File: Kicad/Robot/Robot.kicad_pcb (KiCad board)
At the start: 2 copper layers, 36 parts, among them J1 X8R HEADER, J10 LightBar1, J11 LightBar2, J12 PIN HEADER DE0-NANO POWER, J2 LORA, J3 RELAY HEADER, J4 SENSOR 1, J5 SENSOR 2, J6 SENSOR 3, J7 SENSOR 4, J8 MotorDriver1, J9 MotorDriver2, U1 USB_POWER, U2 Generic_DC_to_DC_Module, U3 Generic_DC_to_DC_Module, U4 Generic_DC_to_DC_Module, U5 Generic_DC_to_DC_Module, U6 X8R_Receiver, U7 TXS0108E, U8 RFM9X, U9 TDB62381A

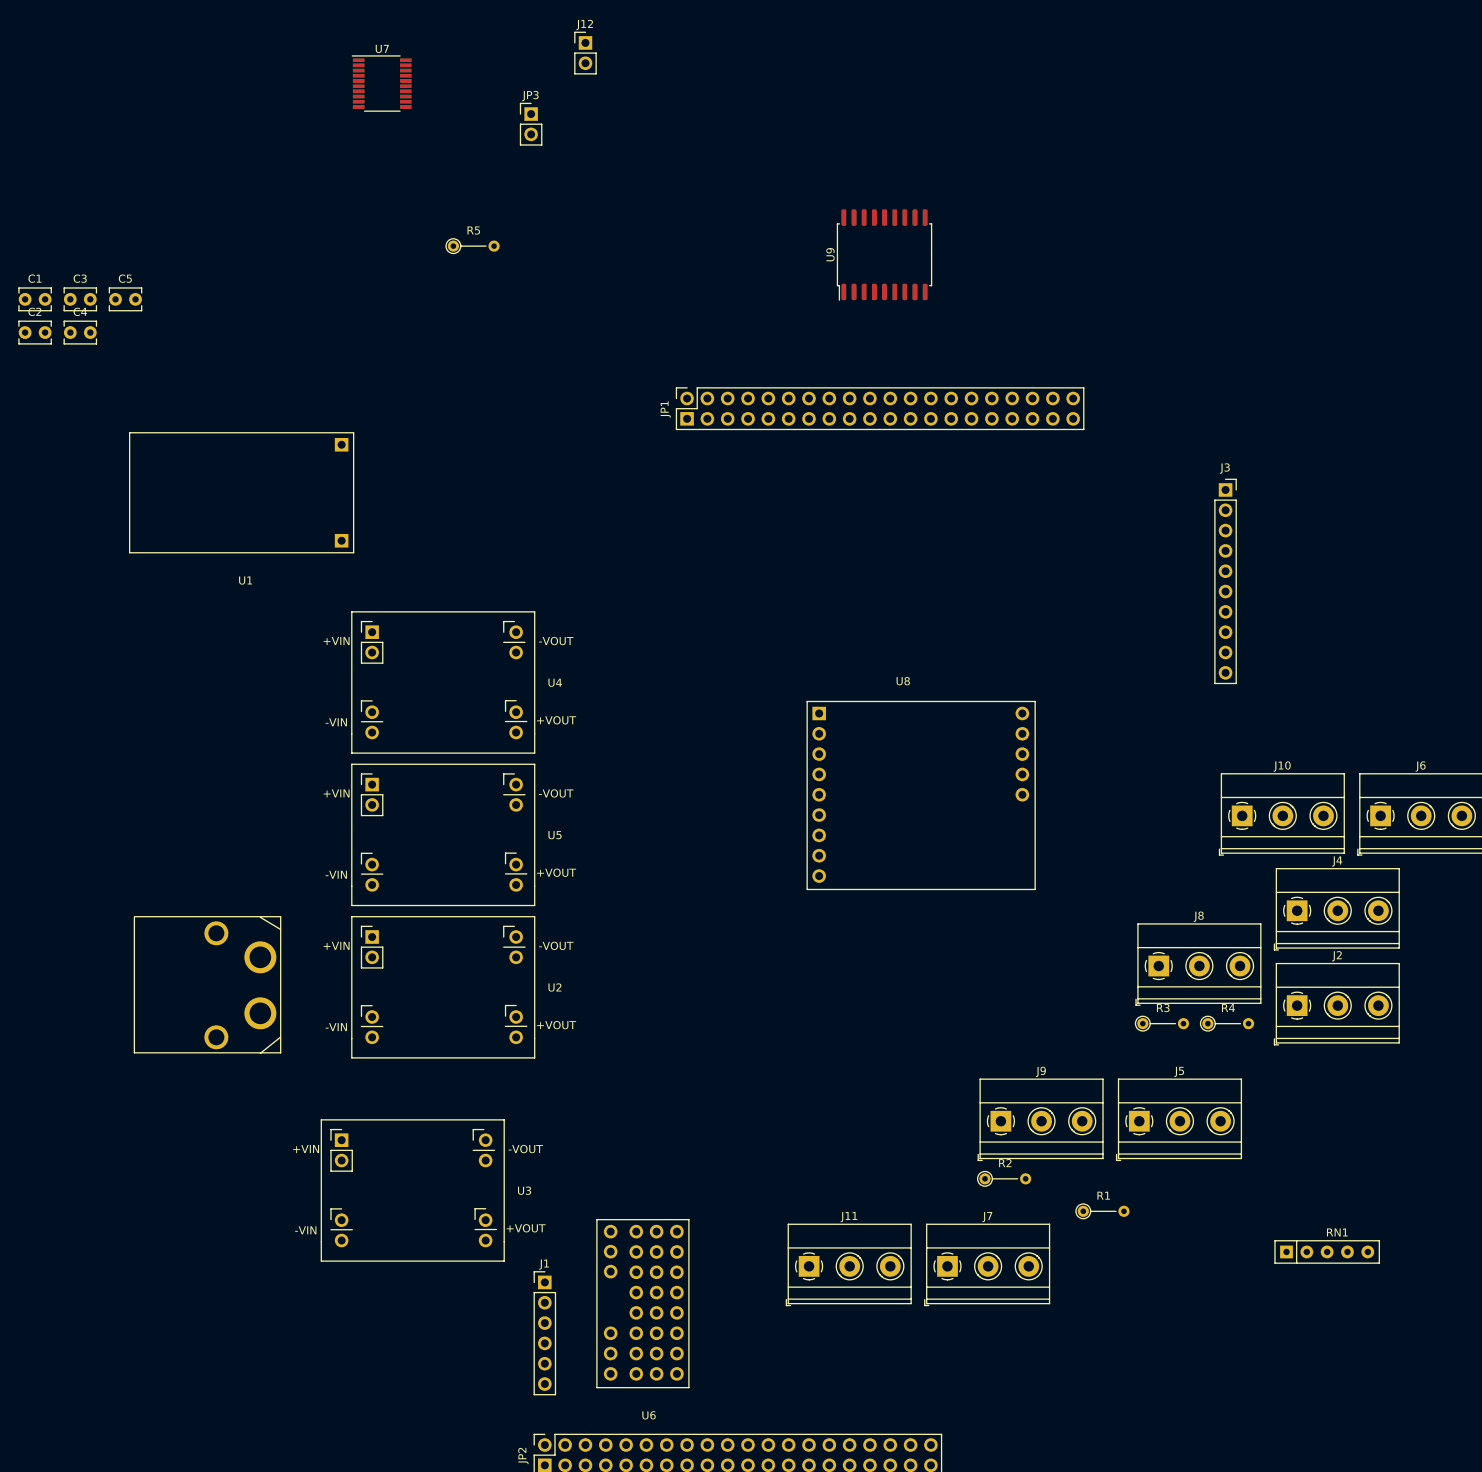
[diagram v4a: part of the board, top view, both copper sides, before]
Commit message: fixed 2 pullups and added cap on output of dc to dc
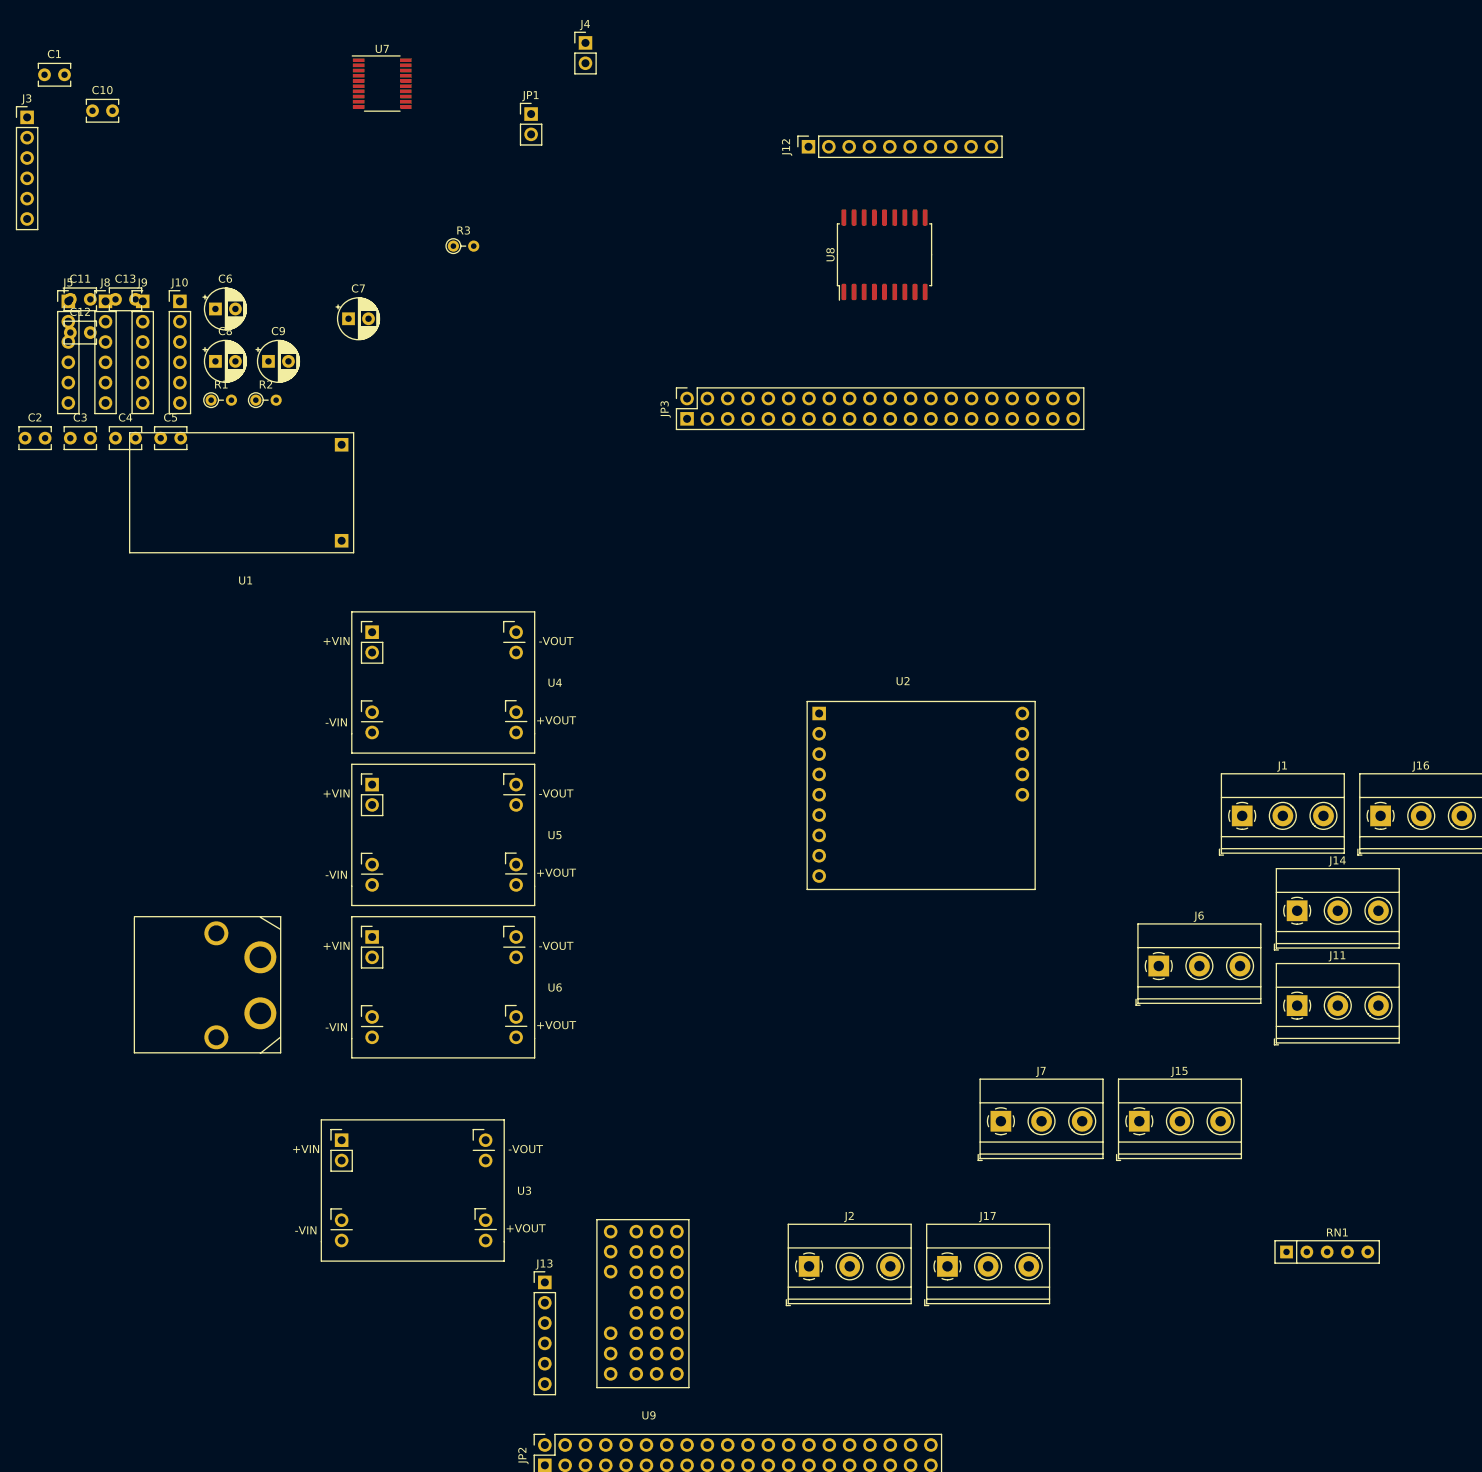
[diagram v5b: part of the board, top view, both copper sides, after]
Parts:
- removed the R3 at (140.8, 92.1)
- removed R4: 4.7k, Robot:R_Axial_DIN0204_L3.6mm_D1.6mm_P5.08mm_Vertical
- added C2: .1uf, Robot:C_Disc_D3.8mm_W2.6mm_P2.50mm, F.Cu at (1.08, 18.9)
- added C3: .1uf, Robot:C_Disc_D3.8mm_W2.6mm_P2.50mm, F.Cu at (6.73, 18.9)
- added C4: .1uf, Robot:C_Disc_D3.8mm_W2.6mm_P2.50mm, F.Cu at (12.4, 18.9)
- added C5: .1uf, Robot:C_Disc_D3.8mm_W2.6mm_P2.50mm, F.Cu at (18.0, 18.9)
- added C6: CP1, Robot:CP_Radial_D5.0mm_P2.50mm, F.Cu at (24.9, 2.78)
- added C7: CP1, Robot:CP_Radial_D5.0mm_P2.50mm, F.Cu at (41.5, 4.00)
- added C8: CP1, Robot:CP_Radial_D5.0mm_P2.50mm, F.Cu at (24.9, 9.33)
- added C9: CP1, Robot:CP_Radial_D5.0mm_P2.50mm, F.Cu at (31.5, 9.33)
- added J10: BreakoutHeader, Robot:PinHeader_1x06_P2.54mm_Vertical, F.Cu at (20.4, 1.83)
- added J3: BreakoutHeader, Robot:PinHeader_1x06_P2.54mm_Vertical, F.Cu at (1.33, -21.2)
- added J5: BreakoutHeader, Robot:PinHeader_1x06_P2.54mm_Vertical, F.Cu at (6.48, 1.83)
- added J8: BreakoutHeader, Robot:PinHeader_1x06_P2.54mm_Vertical, F.Cu at (11.1, 1.83)
- added J9: BreakoutHeader, Robot:PinHeader_1x06_P2.54mm_Vertical, F.Cu at (15.8, 1.83)
- J1: renamed from J10; value LightBar1 -> PositiveBus
- J2: renamed from J11; value LightBar2 -> NegativeBus
- R1, R2: footprint Robot:R_Axial_DIN0204_L3.6mm_D1.6mm_P5.08mm_Vertical -> Robot:R_Axial_DIN0204_L3.6mm_D1.6mm_P2.54mm_Vertical
- R3: renamed from R5; footprint Robot:R_Axial_DIN0204_L3.6mm_D1.6mm_P5.08mm_Vertical -> Robot:R_Axial_DIN0204_L3.6mm_D1.6mm_P2.54mm_Vertical
- moved R1 148.9 mm to (24.3, 14.2)
- moved R2 133.3 mm to (29.9, 14.2)
- moved J12 67.5 mm to (99.0, -17.5), turned to 90 degrees
- moved C10 29.0 mm to (9.50, -22.0)
- moved C1 28.2 mm to (3.50, -26.5)
- renumbered C2 to C10, C3 to C11, C4 to C12, C5 to C13, J2 to J11, J3 to J12, J1 to J13, J4 to J14, J5 to J15, J6 to J16, J7 to J17, J12 to J4, J8 to J6, J9 to J7, JP3 to JP1, JP1 to JP3, U8 to U2, U2 to U6, U9 to U8, U6 to U9
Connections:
- J1 pad 1: Net-(J10-Pad1) (its old number) -> Net-(J1-Pad1)
- J1 pad 2: Net-(J10-Pad2) (its old number) -> Net-(J1-Pad1)
- J1 pad 3: Net-(J10-Pad3) (its old number) -> Net-(J1-Pad1)
- J16 pad 2: Net-(J6-Pad2) (its old number) -> Net-(J16-Pad2)
- J17 pad 2: Net-(J7-Pad2) (its old number) -> Net-(J17-Pad2)
- J2 pad 1: Net-(J10-Pad1) (its old number) -> Net-(J2-Pad1)
- J2 pad 2: Net-(J11-Pad2) -> Net-(J2-Pad1)
- J2 pad 3: Net-(J10-Pad3) (its old number) -> Net-(J2-Pad1)
- JP1 pad 1: Net-(J10-Pad3) (its old number) -> Net-(J1-Pad1)
- JP3 pad 38: Net-(J6-Pad2) (its old number) -> Net-(J16-Pad2)
- JP3 pad 40: Net-(J7-Pad2) (its old number) -> Net-(J17-Pad2)
- POWER_INPUT1 pad 1: Net-(J10-Pad1) (its old number) -> Net-(J2-Pad1)
- POWER_INPUT1 pad 2: Net-(J10-Pad3) (its old number) -> Net-(J1-Pad1)
- R1 pad 1: /3v_pullup -> /VCC3P3
- R1 pad 2: Net-(J7-Pad2) (its old number) -> Net-(JP2-Pad13)
- R2 pad 1: /3v_pullup -> /VCC3P3
- R2 pad 2: Net-(J6-Pad2) (its old number) -> Net-(JP2-Pad15)
- R3 pad 1: Net-(JP2-Pad30) -> Net-(JP2-Pad32)
- RN1 pad 4: Net-(J6-Pad2) (its old number) -> Net-(J16-Pad2)
- RN1 pad 5: Net-(J7-Pad2) (its old number) -> Net-(J17-Pad2)
- U1 pad 1: Net-(J10-Pad3) (its old number) -> Net-(J1-Pad1)
- U1 pad 2: Net-(J10-Pad1) (its old number) -> Net-(J2-Pad1)
- U3 pad 1: Net-(J10-Pad1) (its old number) -> Net-(J2-Pad1)
- U3 pad 2: Net-(J10-Pad1) (its old number) -> Net-(J2-Pad1)
- U3 pad 3: Net-(J10-Pad3) (its old number) -> Net-(J1-Pad1)
- U3 pad 4: Net-(J10-Pad3) (its old number) -> Net-(J1-Pad1)
- U3 pad 7: /PWR_8CH_RLY -> Net-(C2-Pad1)
- U3 pad 8: /PWR_8CH_RLY -> Net-(C2-Pad1)
- U4 pad 1: Net-(J10-Pad1) (its old number) -> Net-(J2-Pad1)
- U4 pad 2: Net-(J10-Pad1) (its old number) -> Net-(J2-Pad1)
- U4 pad 3: Net-(J10-Pad3) (its old number) -> Net-(J1-Pad1)
- U4 pad 4: Net-(J10-Pad3) (its old number) -> Net-(J1-Pad1)
- U5 pad 1: Net-(J10-Pad1) (its old number) -> Net-(J2-Pad1)
- U5 pad 2: Net-(J10-Pad1) (its old number) -> Net-(J2-Pad1)
- U5 pad 3: Net-(J10-Pad3) (its old number) -> Net-(J1-Pad1)
- U5 pad 4: Net-(J10-Pad3) (its old number) -> Net-(J1-Pad1)
- U6 pad 1: Net-(J10-Pad1) (its old number) -> Net-(J2-Pad1)
- U6 pad 2: Net-(J10-Pad1) (its old number) -> Net-(J2-Pad1)
- U7 pad 10: Net-(JP2-Pad30) -> Net-(JP2-Pad32)

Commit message: placed header
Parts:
- moved J4 193.5 mm to (-119.9, 0.52)
- moved JP3 193.5 mm to (-126.7, 9.41)
- moved JP1 149.6 mm to (16.0, 3.84)
- moved J10 148.0 mm to (152.6, -64.8)
- moved C13 146.5 mm to (143.6, -63.5)
- moved C11 146.0 mm to (137.7, -63.1)
- moved C10 142.9 mm to (140.5, -79.0)
- moved C12 142.9 mm to (137.7, -51.2)
- moved C2 142.9 mm to (132.1, -38.0)
- moved C3 142.9 mm to (137.7, -38.0)
- moved C4 142.9 mm to (143.4, -38.0)
- moved C5 142.9 mm to (149.0, -38.0)
- moved C7 142.9 mm to (172.5, -53.0)
- moved C8 142.9 mm to (155.9, -47.6)
- moved C9 142.9 mm to (162.5, -47.6)
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- renumbered JP2 to JP1, JP3 to JP2, JP1 to JP3
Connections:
- U9 pad 1: Net-(U7-Pad20) -> Net-(U7-Pad12)
- U9 pad 2: Net-(U7-Pad18) -> Net-(U7-Pad13)
- U9 pad 3: Net-(U7-Pad17) -> Net-(U7-Pad14)
- U9 pad 4: Net-(U7-Pad16) -> Net-(U7-Pad15)
- U9 pad 5: Net-(U7-Pad15) -> Net-(U7-Pad16)
- U9 pad 6: Net-(U7-Pad14) -> Net-(U7-Pad17)
- U9 pad 7: Net-(U7-Pad13) -> Net-(U7-Pad18)
- U9 pad 8: Net-(U7-Pad12) -> Net-(U7-Pad20)
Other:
- board outline added: 77 x 49 mm

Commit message: Parts placement plus other changes
parts placement plus other changes
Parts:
- removed the J8 at (142.1, -55.1)
- removed RN1: R_Network04, Robot:R_Array_SIP5
- added R4: 4.7K, Robot:R_Axial_DIN0204_L3.6mm_D1.6mm_P2.54mm_Vertical, F.Cu at (74.8, -5.80)
- added R5: 4.7K, Robot:R_Axial_DIN0204_L3.6mm_D1.6mm_P2.54mm_Vertical, F.Cu at (72.8, 10.2)
- added R6: 4.7K, Robot:R_Axial_DIN0204_L3.6mm_D1.6mm_P2.54mm_Vertical, F.Cu at (74.9, 38.1)
- added R7: 4.7K, Robot:R_Axial_DIN0204_L3.6mm_D1.6mm_P2.54mm_Vertical, F.Cu at (72.3, 55.3)
- moved C7 199.6 mm to (-6.40, 35.6), turned to 90 degrees
- moved C6 175.4 mm to (-4.95, 54.5), turned to 90 degrees
- moved C8 174.3 mm to (-6.60, 15.6), turned to 90 degrees
- moved C9 174.1 mm to (-5.95, -3.65), turned to 90 degrees
- moved R3 171.1 mm to (31.9, 12.9), turned to 270 degrees
- moved J8 169.3 mm to (16.0, 52.3), turned to 90 degrees
- moved C3 162.8 mm to (-4.70, 40.9)
- moved C2 160.4 mm to (1.10, 54.5), turned to 90 degrees
- moved R2 159.7 mm to (8.20, 3.85)
- moved J1 158.3 mm to (-57.2, 2.00), turned to 90 degrees
- moved C4 154.6 mm to (-1.75, 15.3), turned to 90 degrees
- moved J9 153.9 mm to (41.3, 41.5), turned to 270 degrees
- moved R1 153.5 mm to (8.25, 1.30)
- moved C5 152.4 mm to (0.60, -3.55), turned to 90 degrees
- moved C10 131.7 mm to (45.9, 12.7), turned to 270 degrees
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- renumbered C13 to C11, C11 to C12, C12 to C13, J11 to J10, J12 to J11, J13 to J12, J14 to J13, J15 to J14, J16 to J15, J17 to J16, J4 to J3, J3 to J4, J9 to J8, J10 to J9
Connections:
- net Net-(J11-Pad1) renamed RX
- C1 pad 1: /PWR_X8R -> PWR_8XR
- C10 pad 1: /VCC3P3 -> VCC3P3
- C11 pad 1: /PWR_8CH_RLY -> VCC3P3
- C12 pad 1: /PWR_X8R -> PWR_8XR
- C13 pad 1: /PWR_X8R -> PWR_8XR
- C2 pad 1: Net-(C2-Pad1) -> PWR_8CH_RLY
- C4 pad 1: /PWR_INDUCTIVE_SENSORS -> PWR_8XR
- C5 pad 1: /PWR_X8R -> PWR_IND_SENSOR
- C6 pad 1: Net-(C2-Pad1) -> PWR_8CH_RLY
- C8 pad 1: /PWR_INDUCTIVE_SENSORS -> PWR_8XR
- C9 pad 1: /PWR_X8R -> PWR_IND_SENSOR
- J10 pad 3: Net-(J11-Pad3) (its old number) -> TX
- J11 pad 10: /PWR_8CH_RLY -> PWR_8CH_RLY
- J13 pad 1: /PWR_INDUCTIVE_SENSORS -> PWR_IND_SENSOR
- J13 pad 2: Net-(J14-Pad2) -> SENSOR1
- J14 pad 1: /PWR_INDUCTIVE_SENSORS -> PWR_IND_SENSOR
- J14 pad 2: Net-(J15-Pad2) -> SENSOR2
- J15 pad 1: /PWR_INDUCTIVE_SENSORS -> PWR_IND_SENSOR
- J15 pad 2: Net-(J16-Pad2) -> SENSOR3
- J16 pad 1: /PWR_INDUCTIVE_SENSORS -> PWR_IND_SENSOR
- J16 pad 2: Net-(J17-Pad2) -> SENSOR4
- J4 pad 1: Net-(J3-Pad1) -> Net-(J4-Pad1)
- J4 pad 2: Net-(J3-Pad2) -> Net-(J4-Pad2)
- J4 pad 3: Net-(J3-Pad3) -> Net-(J4-Pad3)
- J4 pad 4: Net-(J3-Pad4) -> Net-(J4-Pad4)
- J4 pad 5: Net-(J3-Pad5) -> Net-(J4-Pad5)
- J4 pad 6: /VCC3P3 -> Net-(J4-Pad6)
- J6 pad 1: GND -> Net-(J6-Pad1)
- J6 pad 3: Net-(J6-Pad3) -> GND
- J7 pad 1: GND -> Net-(J7-Pad1)
- J7 pad 3: Net-(J7-Pad3) -> GND
- J8 pad 1: Net-(J9-Pad1) -> Net-(J8-Pad1)
- J8 pad 2: Net-(J9-Pad2) -> Net-(J8-Pad2)
- J8 pad 3: Net-(J9-Pad3) -> Net-(J8-Pad3)
- J8 pad 4: Net-(J9-Pad4) -> Net-(J8-Pad4)
- J8 pad 5: Net-(J9-Pad5) -> Net-(J8-Pad5)
- J8 pad 6: Net-(J9-Pad6) -> Net-(J8-Pad6)
- J9 pad 1: Net-(J10-Pad1) -> Net-(J9-Pad1)
- J9 pad 2: Net-(J10-Pad2) -> Net-(J9-Pad2)
- J9 pad 3: Net-(J10-Pad3) -> Net-(J9-Pad3)
- J9 pad 4: Net-(J10-Pad4) -> Net-(J9-Pad4)
- J9 pad 5: Net-(J10-Pad5) -> Net-(J9-Pad5)
- J9 pad 6: Net-(J10-Pad6) -> VCC3P3
- JP1 pad 1: Net-(J5-Pad6) -> CS
- JP1 pad 10: Net-(JP1-Pad10) -> Net-(J5-Pad4)
- JP1 pad 11: Net-(J5-Pad1) -> EN
- JP1 pad 12: Net-(JP1-Pad12) -> Net-(J5-Pad3)
- JP1 pad 14: Net-(JP1-Pad14) -> Net-(J5-Pad2)
- JP1 pad 16: Net-(JP1-Pad16) -> Net-(J5-Pad1)
- JP1 pad 2: Net-(JP1-Pad2) -> RST
- JP1 pad 20: Net-(JP1-Pad20) -> Net-(J4-Pad6)
- JP1 pad 22: Net-(JP1-Pad22) -> Net-(J4-Pad5)
- JP1 pad 24: Net-(JP1-Pad24) -> Net-(J4-Pad4)
- JP1 pad 26: Net-(JP1-Pad26) -> Net-(J4-Pad3)
- JP1 pad 28: Net-(JP1-Pad28) -> Net-(J4-Pad2)
- JP1 pad 29: /VCC3P3 -> VCC3P3
- JP1 pad 3: Net-(J5-Pad5) -> MOSI
- JP1 pad 30: Net-(JP1-Pad30) -> Net-(J4-Pad1)
- JP1 pad 31: Net-(J3-Pad5) -> Net-(JP1-Pad31)
- JP1 pad 33: Net-(J3-Pad4) -> Net-(JP1-Pad33)
- JP1 pad 35: Net-(J3-Pad3) -> Net-(JP1-Pad35)
- JP1 pad 37: Net-(J3-Pad2) -> SENSOR2
- JP1 pad 39: Net-(J3-Pad1) -> SENSOR1
- JP1 pad 40: Net-(J11-Pad3) (its old number) -> TX
- JP1 pad 5: Net-(J5-Pad4) -> MISO
- JP1 pad 6: Net-(JP1-Pad6) -> Net-(J5-Pad6)
- JP1 pad 7: Net-(J5-Pad3) -> SCK
- JP1 pad 8: Net-(JP1-Pad8) -> Net-(J5-Pad5)
- JP1 pad 9: Net-(J5-Pad2) -> G0
- JP2 pad 1: Net-(J9-Pad6) -> Net-(JP2-Pad1)
- JP2 pad 10: Net-(J10-Pad5) -> Net-(JP2-Pad10)
- JP2 pad 11: Net-(J9-Pad1) -> Net-(JP2-Pad11)
- JP2 pad 12: Net-(J10-Pad6) -> Net-(JP2-Pad12)
- JP2 pad 13: Net-(J6-Pad3) -> Net-(JP2-Pad13)
- JP2 pad 14: Net-(JP2-Pad14) -> Net-(J6-Pad1)
- JP2 pad 15: Net-(J6-Pad2) -> Net-(JP2-Pad15)
- JP2 pad 16: Net-(JP2-Pad16) -> Net-(J6-Pad2)
- JP2 pad 19: Net-(JP2-Pad19) -> Net-(J9-Pad1)
- JP2 pad 2: Net-(J10-Pad1) -> Net-(JP2-Pad2)
- JP2 pad 21: Net-(JP2-Pad21) -> Net-(J9-Pad2)
- JP2 pad 23: Net-(J7-Pad3) -> Net-(J9-Pad3)
- JP2 pad 24: Net-(JP2-Pad24) -> Net-(J7-Pad1)
- JP2 pad 25: Net-(J7-Pad2) -> Net-(J9-Pad4)
- JP2 pad 26: Net-(JP2-Pad26) -> Net-(J7-Pad2)
- JP2 pad 27: Net-(JP2-Pad27) -> Net-(J9-Pad5)
- JP2 pad 29: /3v_pullup -> VCC3P3
- JP2 pad 3: Net-(J9-Pad5) -> Net-(JP2-Pad3)
- JP2 pad 30: Net-(JP2-Pad30) -> Net-(J8-Pad6)
- JP2 pad 32: Net-(JP2-Pad32) -> Net-(J8-Pad5)
- JP2 pad 34: Net-(J14-Pad2) -> Net-(J8-Pad4)
- JP2 pad 36: Net-(J15-Pad2) -> Net-(J8-Pad3)
- JP2 pad 38: Net-(J16-Pad2) -> Net-(J8-Pad2)
- JP2 pad 4: Net-(J10-Pad2) -> Net-(JP2-Pad4)
- JP2 pad 40: Net-(J17-Pad2) -> Net-(J8-Pad1)
- JP2 pad 5: Net-(J9-Pad4) -> Net-(JP2-Pad5)
- JP2 pad 6: Net-(J10-Pad3) -> SENSOR3
- JP2 pad 7: Net-(J9-Pad3) -> Net-(JP2-Pad7)
- JP2 pad 8: Net-(J10-Pad4) -> SENSOR4
- JP2 pad 9: Net-(J9-Pad2) -> Net-(JP2-Pad9)
- R1 pad 1: /VCC3P3 -> VCC3P3
- R1 pad 2: Net-(JP1-Pad13) -> RST
- R2 pad 1: /VCC3P3 -> VCC3P3
- R2 pad 2: Net-(JP1-Pad15) -> CS
- R3 pad 1: Net-(JP1-Pad32) -> Net-(JP1-Pad31)
- U2 pad 1: /PWR_X8R -> PWR_8XR
- U2 pad 3: Net-(JP1-Pad25) -> EN
- U2 pad 4: Net-(JP1-Pad23) -> G0
- U2 pad 5: Net-(JP1-Pad21) -> SCK
- U2 pad 6: Net-(JP1-Pad19) -> MISO
- U2 pad 7: Net-(JP1-Pad17) -> MOSI
- U2 pad 8: Net-(JP1-Pad15) -> CS
- U2 pad 9: Net-(JP1-Pad13) -> RST
- U3 pad 7: Net-(C2-Pad1) -> PWR_8CH_RLY
- U3 pad 8: Net-(C2-Pad1) -> PWR_8CH_RLY
- U5 pad 7: /PWR_INDUCTIVE_SENSORS -> PWR_8XR
- U5 pad 8: /PWR_INDUCTIVE_SENSORS -> PWR_8XR
- U6 pad 7: /PWR_X8R -> PWR_IND_SENSOR
- U6 pad 8: /PWR_X8R -> PWR_IND_SENSOR
- U7 pad 1: Net-(JP1-Pad14) -> Net-(JP1-Pad27)
- U7 pad 10: Net-(JP1-Pad32) -> Net-(JP1-Pad31)
- U7 pad 19: /PWR_X8R -> PWR_8XR
- U7 pad 2: /VCC3P3 -> VCC3P3
- U7 pad 3: Net-(JP1-Pad16) -> Net-(JP1-Pad25)
- U7 pad 4: Net-(JP1-Pad18) -> Net-(JP1-Pad23)
- U7 pad 5: Net-(JP1-Pad20) -> Net-(JP1-Pad21)
- U7 pad 6: Net-(JP1-Pad22) -> Net-(JP1-Pad19)
- U7 pad 7: Net-(JP1-Pad24) -> Net-(JP1-Pad17)
- U7 pad 8: Net-(JP1-Pad26) -> Net-(JP1-Pad15)
- U7 pad 9: Net-(JP1-Pad28) -> Net-(JP1-Pad13)
- U8 pad 1: Net-(JP2-Pad14) -> Net-(JP2-Pad15)
- U8 pad 10: /PWR_8CH_RLY -> VCC3P3
- U8 pad 2: Net-(JP2-Pad16) -> Net-(JP2-Pad13)
- U8 pad 3: Net-(JP2-Pad18) -> Net-(JP2-Pad11)
- U8 pad 4: Net-(JP2-Pad20) -> Net-(JP2-Pad9)
- U8 pad 5: Net-(JP2-Pad22) -> Net-(JP2-Pad7)
- U8 pad 6: Net-(JP2-Pad24) -> Net-(JP2-Pad5)
- U8 pad 7: Net-(JP2-Pad26) -> Net-(JP2-Pad3)
- U8 pad 8: Net-(JP2-Pad28) -> Net-(JP2-Pad1)
- U9 pad 10: /PWR_X8R -> PWR_8XR
- U9 pad 11: /PWR_X8R -> PWR_8XR
- U9 pad 12: /PWR_X8R -> PWR_8XR
- U9 pad 13: /PWR_X8R -> PWR_8XR
- U9 pad 14: /PWR_X8R -> PWR_8XR
- U9 pad 15: /PWR_X8R -> PWR_8XR
- U9 pad 16: /PWR_X8R -> PWR_8XR
- U9 pad 9: /PWR_X8R -> PWR_8XR
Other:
- board size 77 x 49 mm -> 159 x 76.9 mm

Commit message: changes
changes
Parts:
- moved R1 6.43 mm to (5.09, 6.90), turned to 180 degrees
- moved R2 3.41 mm to (9.99, 6.75), turned to 180 degrees
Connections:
- JP1 pad 1: CS -> Net-(JP1-Pad1)
- JP1 pad 10: Net-(J5-Pad4) -> Net-(JP1-Pad10)
- JP1 pad 11: EN -> Net-(JP1-Pad11)
- JP1 pad 12: Net-(J5-Pad3) -> Net-(J5-Pad6)
- JP1 pad 14: Net-(J5-Pad2) -> Net-(J5-Pad5)
- JP1 pad 16: Net-(J5-Pad1) -> Net-(J5-Pad4)
- JP1 pad 18: Net-(JP1-Pad18) -> Net-(J5-Pad3)
- JP1 pad 2: RST -> MISO
- JP1 pad 20: Net-(J4-Pad6) -> Net-(J5-Pad2)
- JP1 pad 22: Net-(J4-Pad5) -> Net-(J5-Pad1)
- JP1 pad 24: Net-(J4-Pad4) -> Net-(JP1-Pad24)
- JP1 pad 26: Net-(J4-Pad3) -> Net-(J4-Pad6)
- JP1 pad 28: Net-(J4-Pad2) -> Net-(J4-Pad5)
- JP1 pad 3: MOSI -> Net-(JP1-Pad3)
- JP1 pad 30: Net-(J4-Pad1) -> Net-(J4-Pad4)
- JP1 pad 4: Net-(JP1-Pad4) -> MOSI
- JP1 pad 5: MISO -> SCK
- JP1 pad 6: Net-(J5-Pad6) -> RST
- JP1 pad 7: SCK -> G0
- JP1 pad 8: Net-(J5-Pad5) -> CS
- JP1 pad 9: G0 -> EN
- U8 pad 1: Net-(JP2-Pad15) -> Net-(JP2-Pad17)
- U8 pad 2: Net-(JP2-Pad13) -> Net-(JP2-Pad15)
- U8 pad 3: Net-(JP2-Pad11) -> Net-(JP2-Pad13)
- U8 pad 7: Net-(JP2-Pad3) -> Net-(JP2-Pad2)
- U8 pad 8: Net-(JP2-Pad1) -> Net-(JP2-Pad4)
